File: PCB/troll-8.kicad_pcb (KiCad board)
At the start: 2 copper layers, 100 x 100 mm, 94 parts, among them CON301 BARREL_JACK, P101 SPI_EXT, P104 Audio Out, P105 AOUT, SW601 SW_PUSH, SW602 SW_PUSH, SW603 SW_PUSH, SW604 SW_PUSH, SW605 SW_PUSH, SW606 SW_PUSH, SW607 SW_PUSH, SW608 SW_PUSH, U101 4050, U102 74LVC138, U103 arduino_nano, U201 EXBA10P-RES, U202 CAP1188, U203 Keyboard-16, U204 EXBA10P-RES, U205 CAP1188, U301 MCP1824-LDO, U401 MCP3208, U501 SST25VF-FLASH, U502 23A-SRAM, U601 MCP23S18-GPIO-QFN-OPEN_DRAIN, U602 EXBA10P-RES

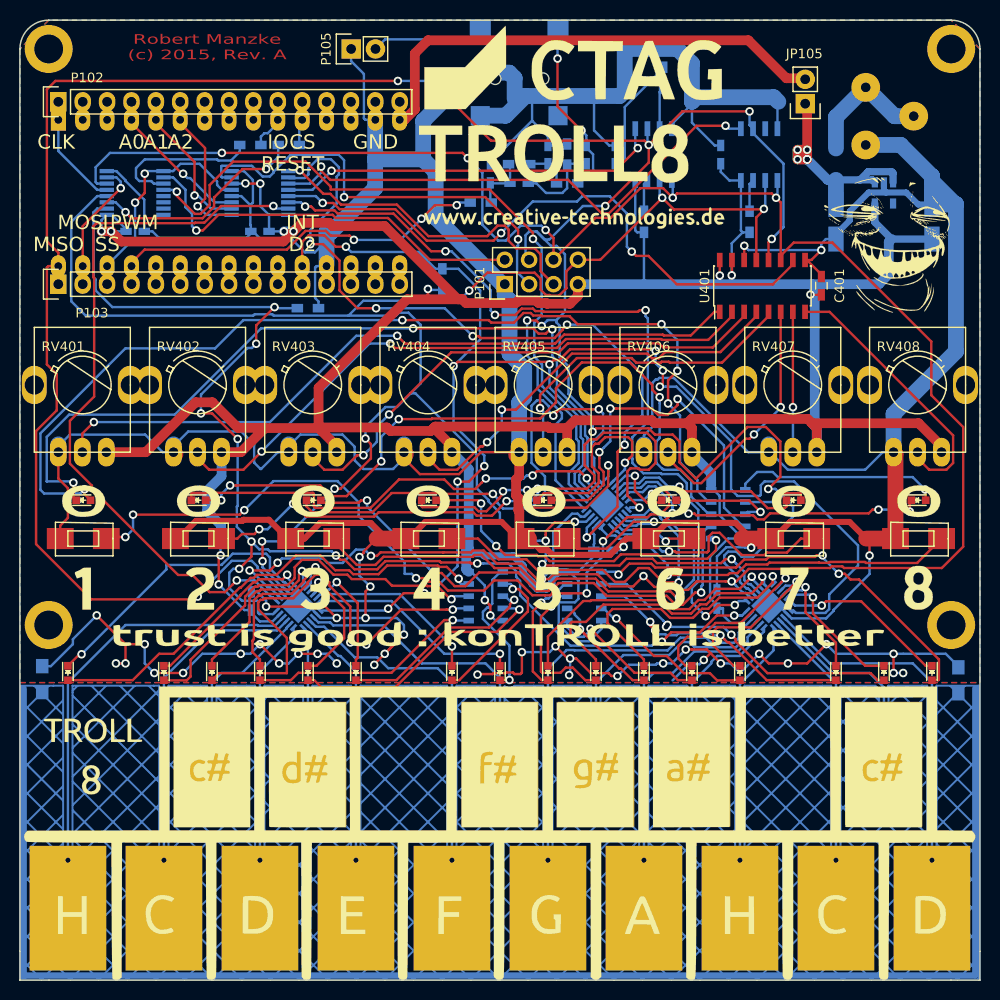
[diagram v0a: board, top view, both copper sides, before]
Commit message: redesign, logo and audio connector changed
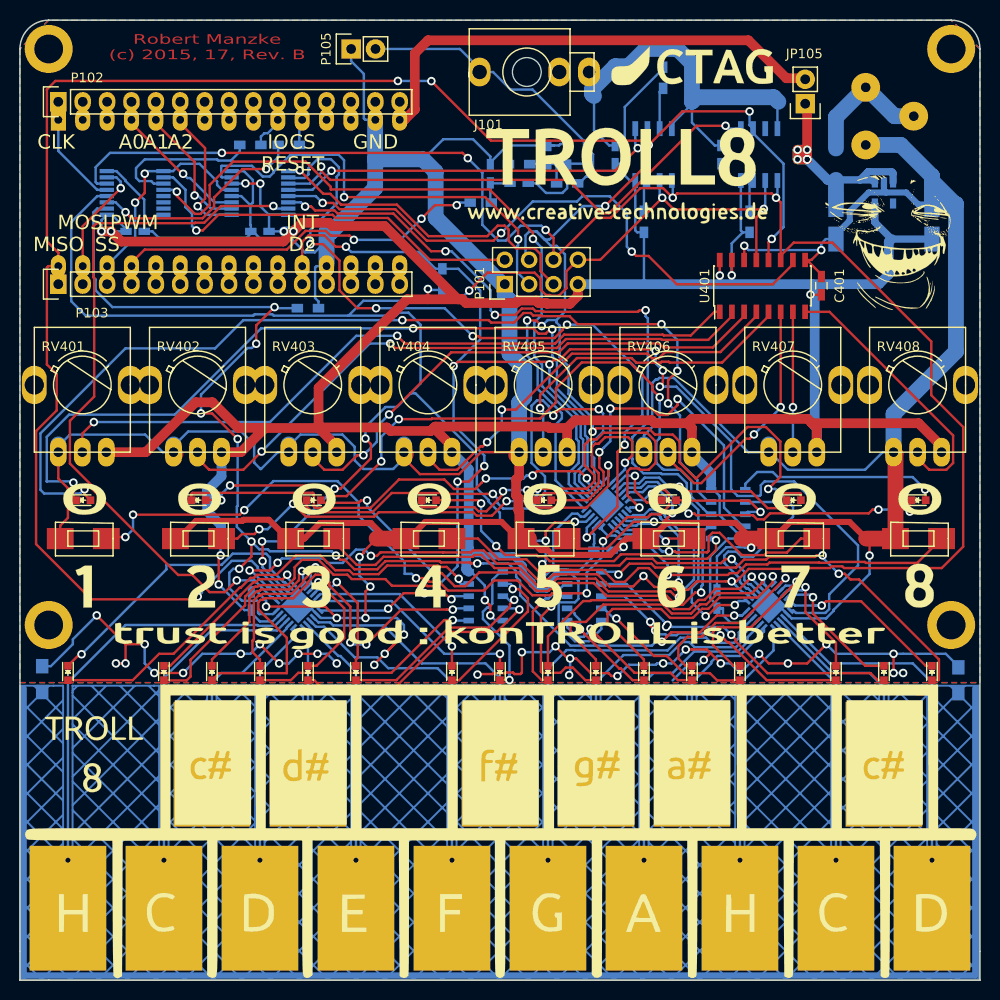
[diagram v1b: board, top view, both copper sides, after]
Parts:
- removed the G*** at (111.1, 97.2)
- removed P104: Audio Out, modules:LUM150302
- added G***: LOGO, troll-8-footprints:Keyboard-Outline, F.Cu at (111.3, 98.6)
- added J101: AUOUT, connectors:THONKICONN, F.Cu at (113.8, 52.4)
- C105: value 200n -> 220n
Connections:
- net /GPIO/INT renamed /INT
- net /GPIO/SPI_CLK renamed /SPI_CLK
- net /GPIO/SPI_MISO renamed /SPI_MISO
- net /GPIO/SPI_MOSI renamed /SPI_MOSI
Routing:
- net GND: track 712.8 -> 687.0 mm
- net Net-(C106-Pad1): track 36.9 -> 31.7 mm, vias 2 -> 0
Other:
- rule pad_to_mask_clearance: 0.0381 -> 0
- board text added: "Robert Manzke (c) 2015, 17, Rev. B"
- board text removed: "Robert Manzke (c) 2015, Rev. A"
